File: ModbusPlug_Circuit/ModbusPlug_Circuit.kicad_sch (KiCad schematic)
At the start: 0 parts

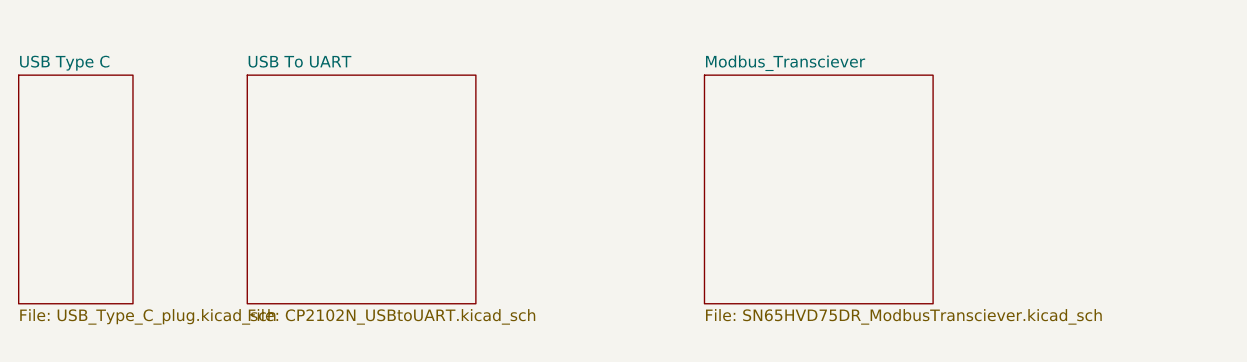
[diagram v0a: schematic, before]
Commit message: Updated USB/PD and TTL circuit
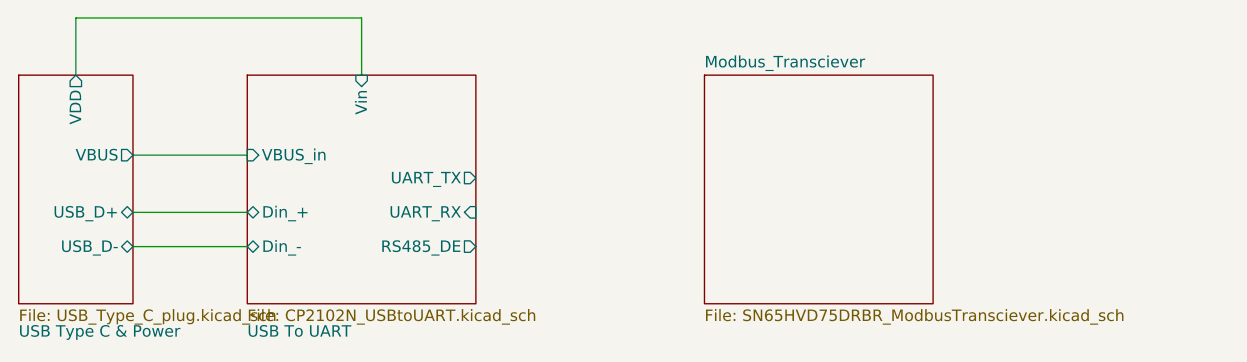
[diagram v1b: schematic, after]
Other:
- sheet USB Type C renamed USB Type C & Power
- sheet Modbus_Transciever: file SN65HVD75DR_ModbusTransciever.kicad_sch -> SN65HVD75DRBR_ModbusTransciever.kicad_sch
- sheet USB To UART ports: added Din_+, Din_-, RS485_DE, UART_RX, UART_TX, VBUS_in, Vin; removed none
- sheet USB Type C & Power ports: added USB_D+, USB_D-, VBUS, VDD; removed none
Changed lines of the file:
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@@
 	(generator_version "9.0")
 	(paper "A4")
+	(wire
+		(pts
+			(xy 82.55 76.2) (xy 82.55 69.85)
+		)
+		(stroke
+			(width 0.8)
+			(type solid)
+			(color 194 0 0 1)
+		)
+	)
+	(wire
+		(pts
+			(xy 82.55 69.85) (xy 114.3 69.85)
+		)
+		(stroke
+			(width 0.8)
+			(type solid)
+			(color 194 0 0 1)
+		)
+	)
+	(wire
+		(pts
+			(xy 88.9 91.44) (xy 101.6 91.44)
+		)
+		(stroke
+			(width 0)
+			(type default)
+			(color 0 255 0 1)
+		)
+	)
+	(wire
+		(pts
+			(xy 88.9 85.09) (xy 101.6 85.09)
+		)
+		(stroke
+			(width 0)
+			(type default)
+			(color 255 0 0 1)
+		)
+	)
+	(wire
+		(pts
+			(xy 114.3 69.85) (xy 114.3 76.2)
+		)
+		(stroke
+			(width 0.8)
+			(type solid)
+			(color 194 0 0 1)
+		)
+	)
+	(wire
+		(pts
+			(xy 88.9 95.25) (xy 101.6 95.25)
+		)
+		(stroke
+			(width 0)
+			(type default)
+			(color 0 255 0 1)
+		)
+	)
 	(sheet
 		(at 76.2 76.2)
@@
 		(on_board yes)
 		(dnp no)
-		(fields_autoplaced yes)
 		(stroke
 			(width 0.1524)
@@
 			(color 0 0 0 0.0000)
 		)
-		(property "Sheetname" "USB Type C"
-			(at 76.2 75.4884 0)
+		(property "Sheetname" "USB Type C & Power"
+			(at 76.2 105.41 0)
 			(effects
 				(font
@@
 				)
 				(justify left top)
+			)
+		)
+		(pin "USB_D+" bidirectional
+			(at 88.9 91.44 0)
+			(effects
+				(font
+					(size 1.27 1.27)
+				)
+				(justify right)
+			)
+		)
+		(pin "USB_D-" bidirectional
+			(at 88.9 95.25 0)
+			(effects
+				(font
+					(size 1.27 1.27)
+				)
+				(justify right)
+			)
+		)
+		(pin "VDD" output
+			(at 82.55 76.2 90)
+			(effects
+				(font
+					(size 1.27 1.27)
+				)
+				(justify right)
+			)
+		)
+		(pin "VBUS" output
+			(at 88.9 85.09 0)
+			(effects
+				(font
+					(size 1.27 1.27)
+				)
+				(justify right)
 			)
 		)
@@
 			)
 		)
-		(property "Sheetfile" "SN65HVD75DR_ModbusTransciever.kicad_sch"
+		(property "Sheetfile" "SN65HVD75DRBR_ModbusTransciever.kicad_sch"
 			(at 152.4 102.1846 0)
 			(effects
@@
 		(on_board yes)
 		(dnp no)
-		(fields_autoplaced yes)
 		(stroke
 			(width 0.1524)
@@
 		)
 		(property "Sheetname" "USB To UART"
-			(at 101.6 75.4884 0)
+			(at 101.6 105.41 0)
 			(effects
 				(font
@@
 			)
 		)
+		(pin "Din_+" bidirectional
+			(at 101.6 91.44 180)
+			(effects
+				(font
+					(size 1.27 1.27)
+				)
+				(justify left)
+			)
+		)
+		(pin "Din_-" bidirectional
+			(at 101.6 95.25 180)
+			(effects
+				(font
+					(size 1.27 1.27)
+				)
+				(justify left)
+			)
+		)
+		(pin "RS485_DE" output
+			(at 127 95.25 0)
+			(effects
+				(font
+					(size 1.27 1.27)
+				)
+				(justify right)
+			)
+		)
+		(pin "UART_RX" input
+			(at 127 91.44 0)
+			(effects
+				(font
+					(size 1.27 1.27)
+				)
+				(justify right)
+			)
+		)
+		(pin "UART_TX" output
+			(at 127 87.63 0)
+			(effects
+				(font
+					(size 1.27 1.27)
+				)
+				(justify right)
+			)
+		)
+		(pin "VBUS_in" input
+			(at 101.6 85.09 180)
+			(effects
+				(font
+					(size 1.27 1.27)
+				)
+				(justify left)
+			)
+		)
+		(pin "Vin" input
+			(at 114.3 76.2 90)
+			(effects
+				(font
+					(size 1.27 1.27)
+				)
+				(justify right)
+			)
+		)

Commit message: pushing V0.1
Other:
- sheet Modbus_Transciever ports: added Vin; removed none
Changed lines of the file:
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@@
 	(generator_version "9.0")
 	(paper "A4")
+	(junction
+		(at 114.3 69.85)
+		(diameter 0)
+		(color 194 0 0 1)
+	)
 	(wire
 		(pts
@@
 	(wire
 		(pts
+			(xy 165.1 69.85) (xy 114.3 69.85)
+		)
+		(stroke
+			(width 0.8)
+			(type default)
+			(color 194 0 0 1)
+		)
+	)
+	(wire
+		(pts
 			(xy 88.9 91.44) (xy 101.6 91.44)
 		)
@@
 			(type default)
 			(color 0 255 0 1)
+		)
+	)
+	(wire
+		(pts
+			(xy 165.1 76.2) (xy 165.1 69.85)
+		)
+		(stroke
+			(width 0.8)
+			(type default)
+			(color 194 0 0 1)
 		)
 	)
@@
 			)
 		)
+		(pin "Vin" input
+			(at 165.1 76.2 90)
+			(effects
+				(font
+					(size 1.27 1.27)
+				)
+				(justify right)
+			)
+		)

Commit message: pushing V0.1.1
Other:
- sheet Modbus_Transciever ports: added 3.3V_in, A+, B-, RS485_D, RS485_DE, RS485_R; removed Vin
- sheet USB To UART ports: added 3.3V_in; removed Vin
- sheet USB Type C & Power ports: added 3.3V_out, VBUS_out; removed VBUS, VDD

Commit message: pushin V0.1.2
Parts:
- added J1, J2: Conn_01x01_Pin, Connector_Wire:SolderWirePad_1x01_SMD_1x2mm, symbol Connector:Conn_01x01_Pin
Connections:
- net Modbus_Transciever/A+: now also J1.1 (Pin_1)
- net Modbus_Transciever/B-: now also J2.1 (Pin_1)
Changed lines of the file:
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@@
+	(wire
+		(pts
+			(xy 177.8 95.25) (xy 194.31 95.25)
+		)
+		(stroke
+			(width 0)
+			(type default)
+		)
+	)
 	(wire
 		(pts
@@
 			(type default)
 			(color 194 0 0 1)
+		)
+	)
+	(wire
+		(pts
+			(xy 177.8 87.63) (xy 194.31 87.63)
+		)
+		(stroke
+			(width 0)
+			(type default)
 		)
 	)
@@
 	)
 	(symbol
+		(lib_id "Connector:Conn_01x01_Pin")
+		(at 199.39 87.63 180)
+		(unit 1)
+		(exclude_from_sim no)
+		(in_bom yes)
+		(on_board yes)
+		(dnp no)
+		(fields_autoplaced yes)
+		(property "Reference" "J1"
+			(at 198.755 82.55 0)
+			(effects
+				(font
+					(size 1.27 1.27)
+				)
+			)
+		)
+		(property "Value" "Conn_01x01_Pin"
+			(at 198.755 85.09 0)
+			(effects
+				(font
+					(size 1.27 1.27)
+				)
+			)
+		)
+		(property "Footprint" "Connector_Wire:SolderWirePad_1x01_SMD_1x2mm"
+			(at 199.39 87.63 0)
+			(effects
+				(font
+					(size 1.27 1.27)
+				)
+				(hide yes)
+			)
+		)
+		(property "Datasheet" "~"
+			(at 199.39 87.63 0)
+			(effects
+				(font
+					(size 1.27 1.27)
+				)
+				(hide yes)
+			)
+		)
+		(property "Description" "Generic connector, single row, 01x01, script generated"
+			(at 199.39 87.63 0)
+			(effects
+				(font
+					(size 1.27 1.27)
+				)
+				(hide yes)
+			)
+		)
+		(pin "1"
+		)
+		(instances
+			(project ""
+				(path "/fd9cd8db-e183-481d-a9fb-02d7f841de3e"
+					(reference "J1")
+					(unit 1)
+				)
+			)
+		)
+	)
+	(symbol
 		(lib_id "power:+3.3V")
 		(at 66.04 69.85 0)
@@
 					(unit 1)
 				)
+			)
+		)
+	)
+	(symbol
+		(lib_id "Connector:Conn_01x01_Pin")
+		(at 199.39 95.25 180)
+		(unit 1)
+		(exclude_from_sim no)
+		(in_bom yes)
+		(on_board yes)
+		(dnp no)
+		(fields_autoplaced yes)
+		(property "Reference" "J2"
+			(at 198.755 90.17 0)
+			(effects
+				(font
+					(size 1.27 1.27)
+				)
+			)
+		)
+		(property "Value" "Conn_01x01_Pin"
+			(at 198.755 92.71 0)
+			(effects
+				(font
+					(size 1.27 1.27)
+				)
+			)
+		)
+		(property "Footprint" "Connector_Wire:SolderWirePad_1x01_SMD_1x2mm"
+			(at 199.39 95.25 0)
+			(effects
+				(font
+					(size 1.27 1.27)
+				)
+				(hide yes)
+			)
+		)
+		(property "Datasheet" "~"
+			(at 199.39 95.25 0)
+			(effects
+				(font
+					(size 1.27 1.27)
+				)
+				(hide yes)
+			)
+		)
+		(property "Description" "Generic connector, single row, 01x01, script generated"
+			(at 199.39 95.25 0)
+			(effects
+				(font
+					(size 1.27 1.27)
+				)
+				(hide yes)
+			)
+		)
+		(pin "1"
+		)
+		(instances
+			(project "ModbusPlug_Circuit"
+				(path "/fd9cd8db-e183-481d-a9fb-02d7f841de3e"
+					(reference "J2")
+					(unit 1)
+				)

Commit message: pushing V0.1.3
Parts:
- added J3: Conn_01x01_Pin, Connector_Wire:SolderWirePad_1x01_SMD_1x2mm, symbol Connector:Conn_01x01_Pin
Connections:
- new net GND: J3.1 (Pin_1)
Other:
- moved on the sheet: J1, J2
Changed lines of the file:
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@@
 	(wire
 		(pts
-			(xy 177.8 95.25) (xy 194.31 95.25)
+			(xy 177.8 88.9) (xy 194.31 88.9)
 		)
 		(stroke
@@
 	(wire
 		(pts
-			(xy 177.8 87.63) (xy 194.31 87.63)
+			(xy 194.31 96.52) (xy 190.5 96.52)
+		)
+		(stroke
+			(width 0)
+			(type default)
+		)
+	)
+	(wire
+		(pts
+			(xy 190.5 96.52) (xy 190.5 99.06)
+		)
+		(stroke
+			(width 0)
+			(type default)
+		)
+	)
+	(wire
+		(pts
+			(xy 177.8 81.28) (xy 194.31 81.28)
 		)
 		(stroke
@@
 	(symbol
 		(lib_id "Connector:Conn_01x01_Pin")
-		(at 199.39 87.63 180)
+		(at 199.39 81.28 180)
 		(unit 1)
 		(exclude_from_sim no)
@@
 		(fields_autoplaced yes)
 		(property "Reference" "J1"
-			(at 198.755 82.55 0)
+			(at 198.755 76.2 0)
 			(effects
 				(font
@@
 		)
 		(property "Value" "Conn_01x01_Pin"
-			(at 198.755 85.09 0)
+			(at 198.755 78.74 0)
 			(effects
 				(font
@@
 		)
 		(property "Footprint" "Connector_Wire:SolderWirePad_1x01_SMD_1x2mm"
-			(at 199.39 87.63 0)
+			(at 199.39 81.28 0)
 			(effects
 				(font
@@
 		)
 		(property "Datasheet" "~"
-			(at 199.39 87.63 0)
+			(at 199.39 81.28 0)
 			(effects
 				(font
@@
 		)
 		(property "Description" "Generic connector, single row, 01x01, script generated"
-			(at 199.39 87.63 0)
+			(at 199.39 81.28 0)
 			(effects
 				(font
@@
 	(symbol
 		(lib_id "Connector:Conn_01x01_Pin")
-		(at 199.39 95.25 180)
+		(at 199.39 88.9 180)
 		(unit 1)
 		(exclude_from_sim no)
@@
 		(fields_autoplaced yes)
 		(property "Reference" "J2"
-			(at 198.755 90.17 0)
+			(at 198.755 83.82 0)
 			(effects
 				(font
@@
 		)
 		(property "Value" "Conn_01x01_Pin"
-			(at 198.755 92.71 0)
+			(at 198.755 86.36 0)
 			(effects
 				(font
@@
 		)
 		(property "Footprint" "Connector_Wire:SolderWirePad_1x01_SMD_1x2mm"
-			(at 199.39 95.25 0)
+			(at 199.39 88.9 0)
 			(effects
 				(font
@@
 		)
 		(property "Datasheet" "~"
-			(at 199.39 95.25 0)
+			(at 199.39 88.9 0)
 			(effects
 				(font
@@
 		)
 		(property "Description" "Generic connector, single row, 01x01, script generated"
-			(at 199.39 95.25 0)
+			(at 199.39 88.9 0)
 			(effects
 				(font
@@
 				(path "/fd9cd8db-e183-481d-a9fb-02d7f841de3e"
 					(reference "J2")
+					(unit 1)
+				)
+			)
+		)
+	)
+	(symbol
+		(lib_id "Connector:Conn_01x01_Pin")
+		(at 199.39 96.52 180)
+		(unit 1)
+		(exclude_from_sim no)
+		(in_bom yes)
+		(on_board yes)
+		(dnp no)
+		(fields_autoplaced yes)
+		(property "Reference" "J3"
+			(at 198.755 91.44 0)
+			(effects
+				(font
+					(size 1.27 1.27)
+				)
+			)
+		)
+		(property "Value" "Conn_01x01_Pin"
+			(at 198.755 93.98 0)
+			(effects
+				(font
+					(size 1.27 1.27)
+				)
+			)
+		)
+		(property "Footprint" "Connector_Wire:SolderWirePad_1x01_SMD_1x2mm"
+			(at 199.39 96.52 0)
+			(effects
+				(font
+					(size 1.27 1.27)
+				)
+				(hide yes)
+			)
+		)
+		(property "Datasheet" "~"
+			(at 199.39 96.52 0)
+			(effects
+				(font
+					(size 1.27 1.27)
+				)
+				(hide yes)
+			)
+		)
+		(property "Description" "Generic connector, single row, 01x01, script generated"
+			(at 199.39 96.52 0)
+			(effects
+				(font
+					(size 1.27 1.27)
+				)
+				(hide yes)
+			)
+		)
+		(pin "1"
+		)
+		(instances
+			(project "ModbusPlug_Circuit"
+				(path "/fd9cd8db-e183-481d-a9fb-02d7f841de3e"
+					(reference "J3")
 					(unit 1)
 				)
@@
 		)
 	)
+	(symbol
+		(lib_id "power:GND")
+		(at 190.5 99.06 0)
+		(unit 1)
+		(exclude_from_sim no)
+		(in_bom yes)
+		(on_board yes)
+		(dnp no)
+		(fields_autoplaced yes)
+		(property "Reference" "#PWR020"
+			(at 190.5 105.41 0)
+			(effects
+				(font
+					(size 1.27 1.27)
+				)
+				(hide yes)
+			)
+		)
+		(property "Value" "GND"
+			(at 190.5 104.14 0)
+			(effects
+				(font
+					(size 1.27 1.27)
+				)
+			)
+		)
+		(property "Footprint" ""
+			(at 190.5 99.06 0)
+			(effects
+				(font
+					(size 1.27 1.27)
+				)
+				(hide yes)
+			)
+		)
+		(property "Datasheet" ""
+			(at 190.5 99.06 0)
+			(effects
+				(font
+					(size 1.27 1.27)
+				)
+				(hide yes)
+			)
+		)
+		(property "Description" "Power symbol creates a global label with name \"GND\" , ground"
+			(at 190.5 99.06 0)
+			(effects
+				(font
+					(size 1.27 1.27)
+				)
+				(hide yes)
+			)
+		)
+		(pin "1"
+		)
+		(instances
+			(project ""
+				(path "/fd9cd8db-e183-481d-a9fb-02d7f841de3e"
+					(reference "#PWR020")
+					(unit 1)
+				)
+			)
+		)
+	)
 	(sheet
 		(at 63.5 76.2)
@@
 		)
 		(pin "A+" bidirectional
-			(at 177.8 87.63 0)
+			(at 177.8 81.28 0)
 			(effects
 				(font
@@
 		)
 		(pin "B-" bidirectional
-			(at 177.8 95.25 0)
-			(effects
-				(font
+			(at 177.8 88.9 0)
+			(effects
+				(font

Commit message: pushing V0.1.4
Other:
- title: (none) -> ModbusPlug
- moved on the sheet: J1, J2, J3
